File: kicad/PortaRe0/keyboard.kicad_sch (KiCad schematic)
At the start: 158 parts, among them J1 StickSocket, U6 RP2040, U7 W25Q32JVSSIQ, Y2 12Mhz

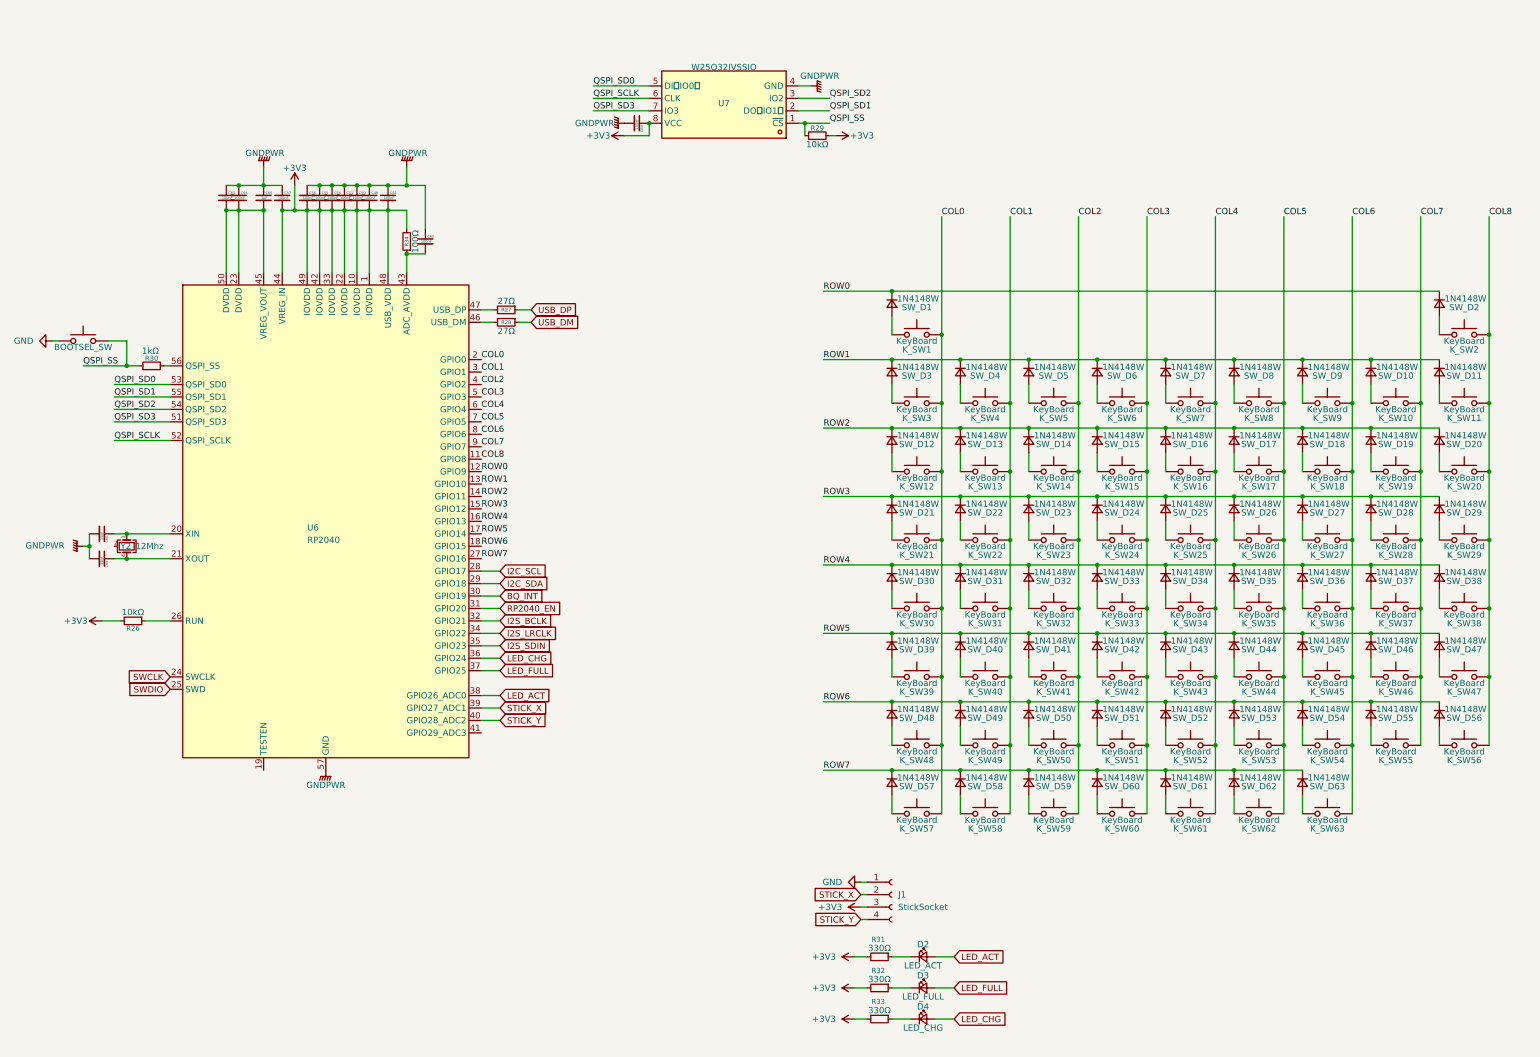
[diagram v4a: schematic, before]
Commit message: session10: audio sheet完成、USB命名規則統一、TESTEN修正
- audio.kicad_sch: RP2040 #2追加、MAX98357A×2、PCM5102APWR、TPA6132A2RTER配線完了
- PCM5102APWR/TPA6132A2RTERシンボル・フットプリント追加
- I2S共有バス(BCLK/LRCLK/SDIN)でスピーカー・イヤホン共通接続
- GPIO割り当て: GP0-2=I2S, GP3=SD_MODE, GP4=XSMT, GP5=HP_EN, GP6=HP_DET
- USB命名規則統一: RP2040 #1→USB2_RP_DP/DM, RP2040 #2→USB2_RP_DP2/DM2
- VL812 USBHP4にUSB2_RP_DP2/DM2追加
- RP2040 #1/#2のTESTEN→GND修正
- BQ25895 D+/D-はUSB_DP/DM(充電用USB-C)で確定

Co-Authored-By: Claude Sonnet 4.6 <noreply@anthropic.com>
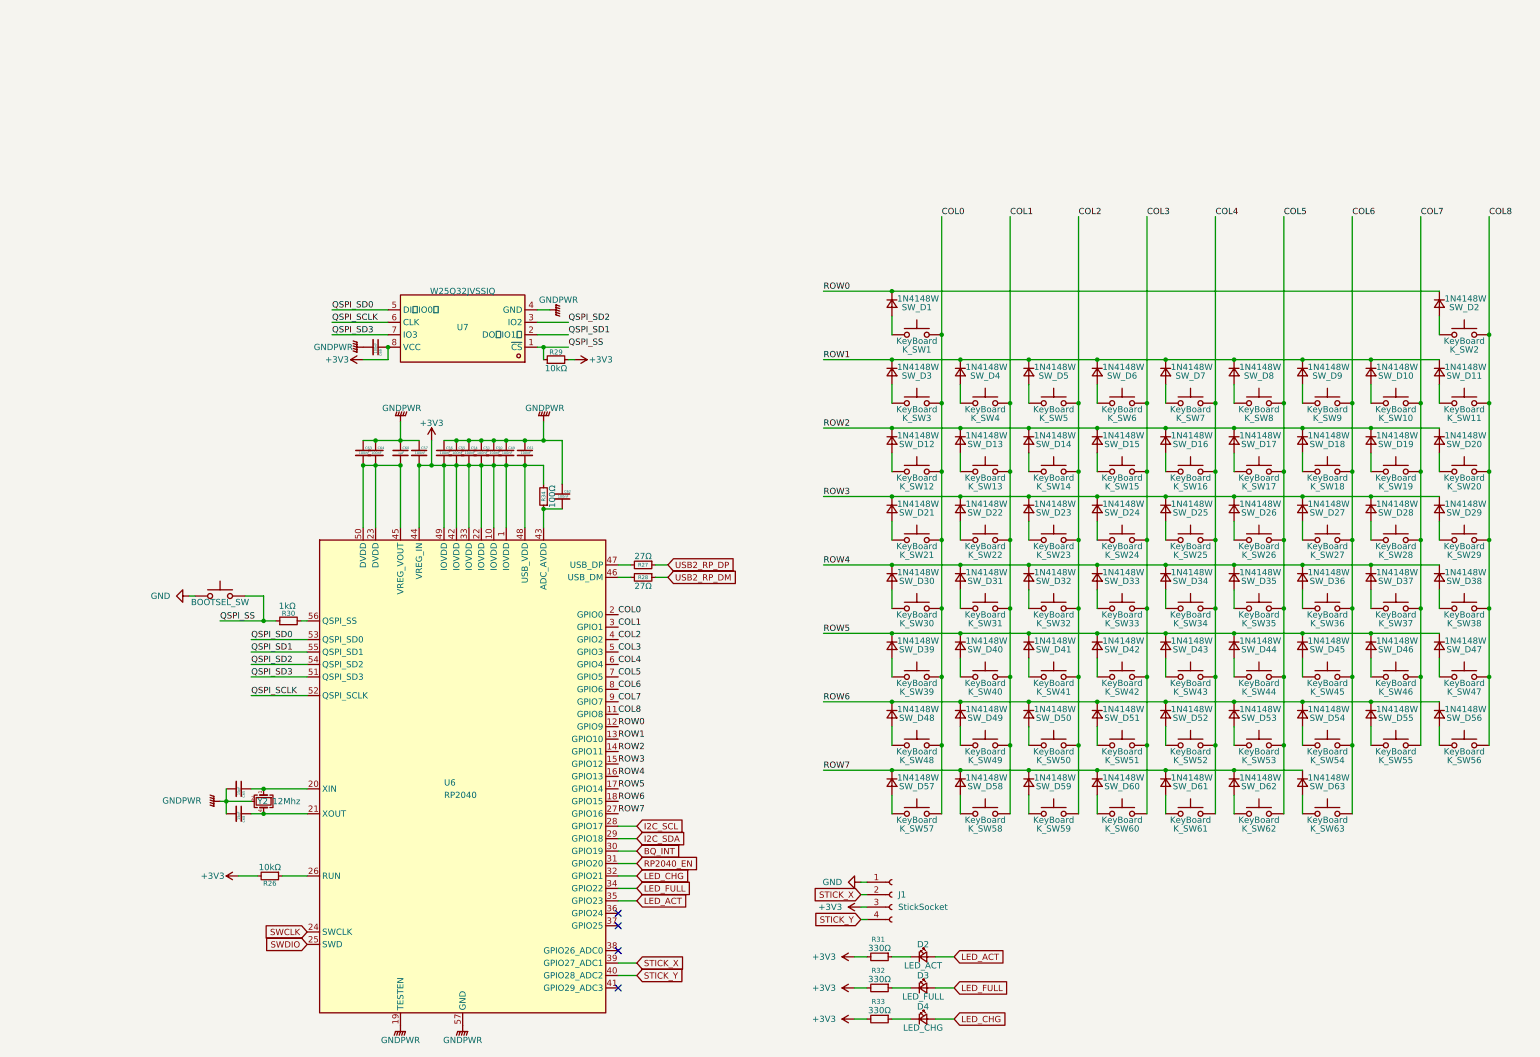
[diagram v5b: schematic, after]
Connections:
- net I2S_BCLK is gone; now on net LED_CHG: U6.32 (GPIO21)
- net I2S_LRCLK is gone; now on net LED_FULL: U6.34 (GPIO22)
- net I2S_SDIN is gone; now on net LED_ACT: U6.35 (GPIO23)
- net GNDPWR: now also U6.19 (TESTEN), Y2.2 (G), Y2.3 (G)
- net LED_ACT: no longer U6.38 (GPIO26_ADC0)
- net LED_CHG: no longer U6.36 (GPIO24)
- net LED_FULL: no longer U6.37 (GPIO25)
- net USB_DM renamed USB2_RP_DM
- net USB_DP renamed USB2_RP_DP
- no-connect marks 0 -> 4
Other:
- moved on the sheet: C49, C50, C51, C54, C55, C56, C57, C60, C61, C62, C63, C64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

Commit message: Fix: Geminiレビュー指摘事項の修正
- audio.kicad_sch: TPA6132A2 HPVSSピンのGND直結を修正（1µFコンデンサ追加）
- audio.kicad_sch: MAX98357A U8のSD_MODEに220kΩ直列抵抗追加（Right ch設定）
- keyboard.kicad_sch: LED回路の向きと接続を修正
- RP2040 #1/#2 TESTEN→GND修正済み確認

Co-Authored-By: Claude Sonnet 4.6 <noreply@anthropic.com>
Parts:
- U6: value RP2040 -> RP2040#1
- renumbered U7 to RP2040#1
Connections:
- net LED_ACT: now also D2.1 (K); no longer D2.2 (A)
- net LED_CHG: now also D4.1 (K); no longer D4.2 (A)
- net LED_FULL: now also D3.1 (K); no longer D3.2 (A)
- net at R32.1: now also D3.2 (A); no longer D3.1 (K)
- net at R33.1: now also D4.2 (A); no longer D4.1 (K)
- net at R31.1: now also D2.2 (A); no longer D2.1 (K)
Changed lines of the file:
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@@
 		(lib_id "Device:LED_Small")
 		(at 201.93 214.63 0)
+		(mirror y)
 		(unit 1)
 		(exclude_from_sim no)
@@
 		(on_board yes)
 		(dnp no)
-		(property "Reference" "U7"
-			(at 107.95 79.756 0)
+		(property "Reference" "RP2040#1"
+			(at 107.95 74.168 0)
 			(effects
 				(font
@@
 			(project ""
 				(path "/479aadc4-f9a0-4ec2-b000-6a17237038f1/6a589eb8-1cb5-4d2d-b60c-ea2cdc8e2546"
-					(reference "U7")
+					(reference "RP2040#1")
 					(unit 1)
 				)
@@
 		(lib_id "Device:LED_Small")
 		(at 201.93 220.98 0)
+		(mirror y)
 		(unit 1)
 		(exclude_from_sim no)
@@
 		(lib_id "Device:LED_Small")
 		(at 201.93 208.28 0)
+		(mirror y)
 		(unit 1)
 		(exclude_from_sim no)
@@
 			)
 		)
-		(property "Value" "RP2040"
+		(property "Value" "RP2040#1"
 			(at 104.14 175.26 0)
 			(effects

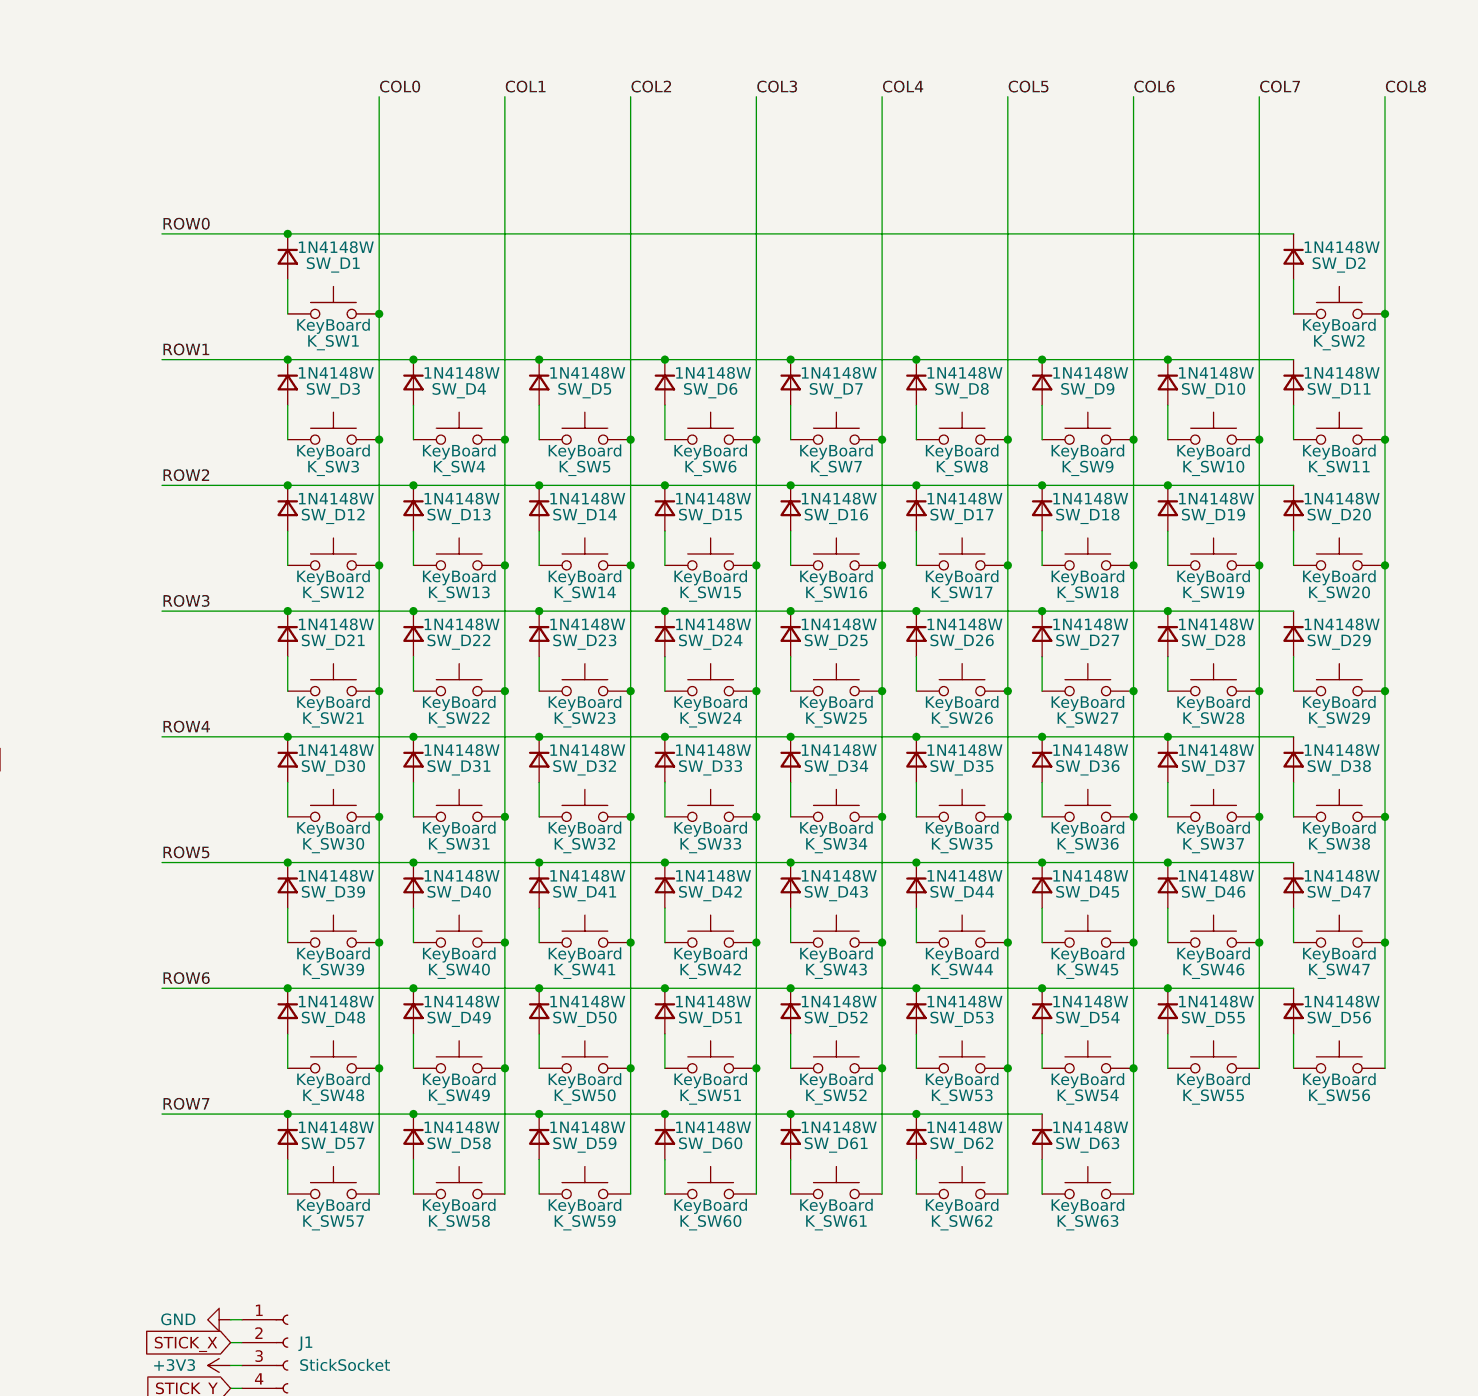
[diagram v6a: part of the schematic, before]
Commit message: Docs: session18終了処理・PROGRESS/index更新・connectorsシート設計方針確定
- J_HDMI_CTRL: 24pin FPC 0.5mm (C2856805) ライブラリ取得・配置方針確定
- SBC接続: サブ基板→FPCに変更・スティフナーにMicro HDMIオス+USB-Cオス直付け方針
- connectors.kicad_sch 追加

Co-Authored-By: Claude Sonnet 4.6 <noreply@anthropic.com>
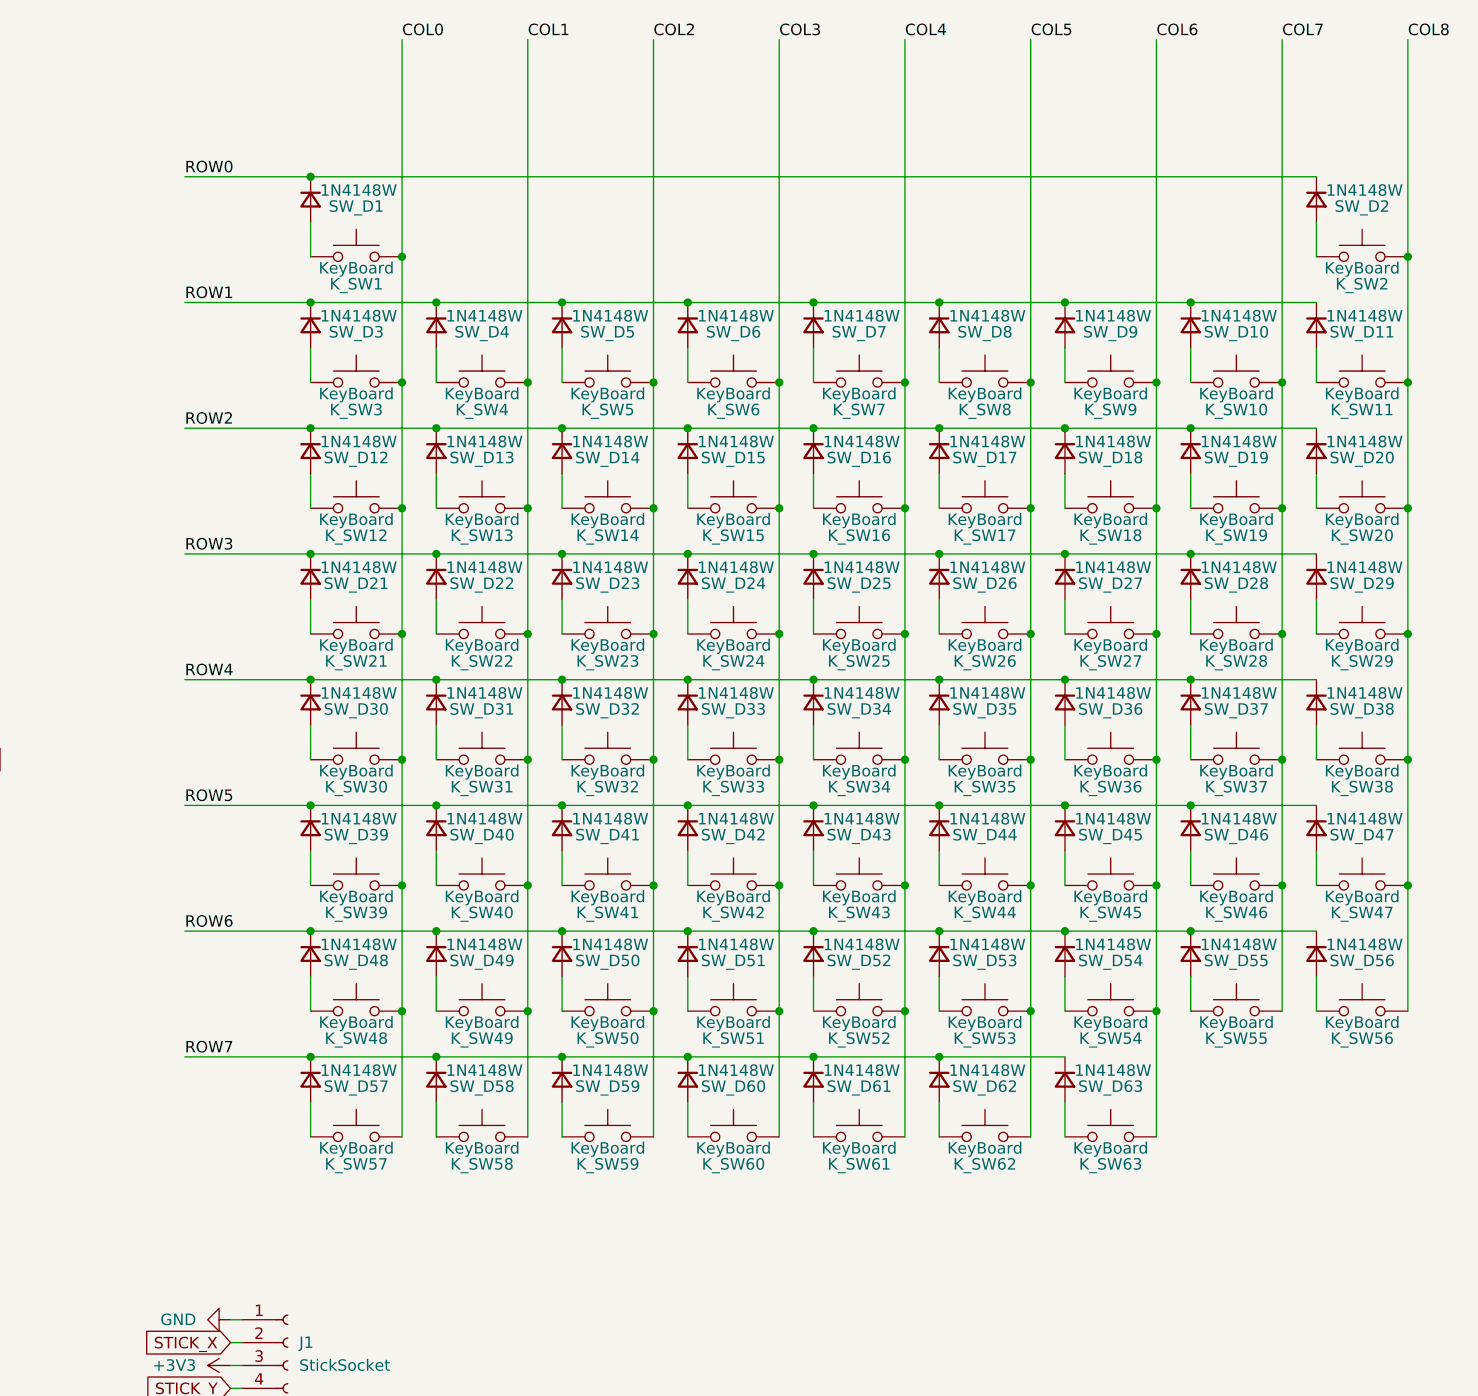
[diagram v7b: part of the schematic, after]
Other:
- moved on the sheet: K_SW1, K_SW10, K_SW11, K_SW12, K_SW13, K_SW14, K_SW15, K_SW16, K_SW17, K_SW18, K_SW19, K_SW2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

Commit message: Docs: session21終了処理・PROGRESS/index更新・connectorsシート完成・ERC対処
- connectors シート完成（J_SBC_HDMI / J_FAN配置完了）
- hdmi_adapter シート新設（別基板 / J_MICROHDMI Conn_02x08 + C2856805）
- J_FAN: F16FB選定（16×16×4.5mm 5V）/ BSS138回路 / FAN_PWM GlobalLabel
- 全シートERC実施・対処完了（VL812未接続ピン / SWD NC / DC10FB追加等）

Co-Authored-By: Claude Sonnet 4.6 <noreply@anthropic.com>
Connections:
- net FAN_PWM: now reaches U6.38 (GPIO26_ADC0)
- net SWCLK: no longer names the net of U6.24 (SWCLK)
- net SWDIO: no longer names the net of U6.25 (SWD)
- no-connect marks 4 -> 5
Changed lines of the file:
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@@
 	)
 	(no_connect
-		(at 139.7 207.01)
+		(at 76.2 203.2)
 	)
 	(no_connect
 		(at 139.7 201.93)
 	)
+	(no_connect
+		(at 76.2 205.74)
+	)
 	(wire
 		(pts
@@
 	(wire
 		(pts
+			(xy 142.24 207.01) (xy 139.7 207.01)
+		)
+		(stroke
+			(width 0)
+			(type default)
+		)
+	)
+	(wire
+		(pts
 			(xy 281.94 135.89) (xy 295.91 135.89)
 		)
@@
 		)
 	)
-	(global_label "SWCLK"
-		(shape input)
-		(at 76.2 203.2 180)
-		(fields_autoplaced yes)
-		(effects
-			(font
-				(size 1.27 1.27)
-			)
-			(justify right)
-		)
-		(property "Intersheetrefs" "${INTERSHEET_REFS}"
-			(at 66.9858 203.2 0)
-			(effects
-				(font
-					(size 1.27 1.27)
-				)
-				(justify right)
-				(hide yes)
-			)
-		)
-	)
 	(global_label "BQ_INT"
 		(shape input)
@@
 		)
 	)
-	(global_label "LED_CHG"
+	(global_label "FAN_PWM"
 		(shape input)
-		(at 143.51 191.77 0)
+		(at 142.24 207.01 0)
 		(fields_autoplaced yes)
 		(effects
@@
 		)
 		(property "Intersheetrefs" "${INTERSHEET_REFS}"
-			(at 154.7804 191.77 0)
+			(at 153.8733 207.01 0)
 			(effects
 				(font
@@
 		)
 	)
-	(global_label "SWDIO"
+	(global_label "LED_CHG"
 		(shape input)
-		(at 76.2 205.74 180)
+		(at 143.51 191.77 0)
 		(fields_autoplaced yes)
 		(effects
@@
 				(size 1.27 1.27)
 			)
-			(justify right)
+			(justify left)
 		)
 		(property "Intersheetrefs" "${INTERSHEET_REFS}"
-			(at 67.3486 205.74 0)
+			(at 154.7804 191.77 0)
 			(effects
 				(font
 					(size 1.27 1.27)
 				)
-				(justify right)
+				(justify left)
 				(hide yes)
 			)
